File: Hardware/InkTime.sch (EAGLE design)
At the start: 105 parts, among them IC1 BQ25180YBGR, IC2 DRV2605YZFR, IC3 BMA423, IC9 RT6160AWSC, J1 503480-2400, J2 TC2030-IDC, J4 KH-TYPE-C-16P, Q1 20V/4.2A/52mΩ/1.4W, Q3 SI1308EDL-T1-GE3, U1 NRF52840_QF, U3 MAX17048G+T10, X1 32MHz, X2 32.768kHz

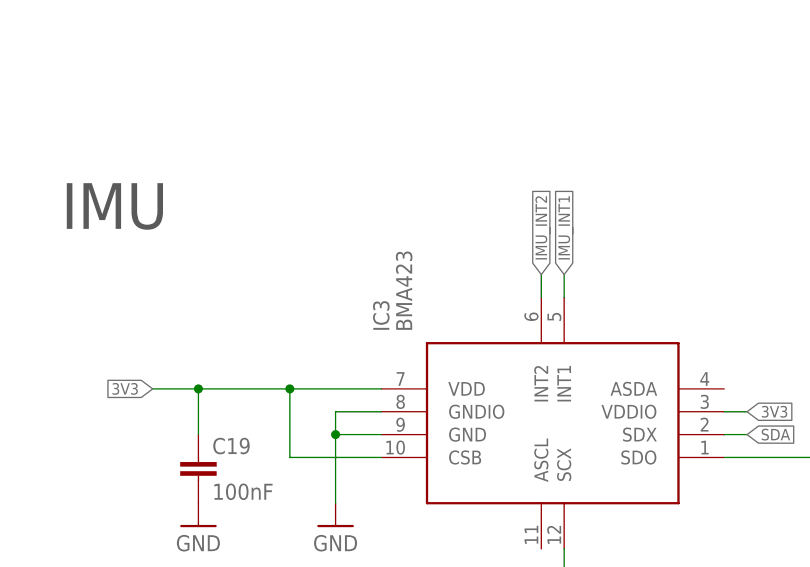
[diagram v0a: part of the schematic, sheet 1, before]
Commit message: fix: BMA423 -> BMA421
Signed-off-by: Luca Mazilescu <luca.mazilescu@protonmail.com>
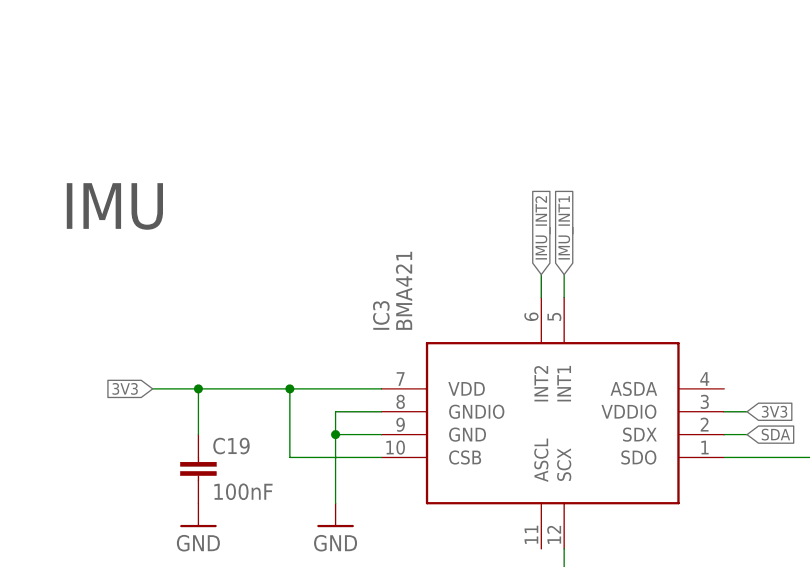
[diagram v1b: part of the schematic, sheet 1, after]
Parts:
- IC3: value BMA423 -> BMA421; device InkTime_v5:BMA423_BMA423 -> InkTime_v5:BMA421_BMA421
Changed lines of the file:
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@@
 <grid distance="0.1" unitdist="inch" unit="inch" style="lines" multiple="1" display="no" altdistance="0.01" altunitdist="inch" altunit="inch"/>
 <layers>
-<layer number="1" name="Top" color="4" fill="1" visible="no" active="no"/>
-<layer number="2" name="Route2" color="16" fill="1" visible="no" active="no"/>
-<layer number="3" name="Route3" color="17" fill="1" visible="no" active="no"/>
-<layer number="4" name="Route4" color="18" fill="1" visible="no" active="no"/>
-<layer number="5" name="Route5" color="19" fill="1" visible="no" active="no"/>
-<layer number="6" name="Route6" color="25" fill="1" visible="no" active="no"/>
-<layer number="7" name="Route7" color="26" fill="1" visible="no" active="no"/>
-<layer number="8" name="Route8" color="27" fill="1" visible="no" active="no"/>
-<layer number="9" name="Route9" color="28" fill="1" visible="no" active="no"/>
-<layer number="10" name="Route10" color="29" fill="1" visible="no" active="no"/>
-<layer number="11" name="Route11" color="30" fill="1" visible="no" active="no"/>
-<layer number="12" name="Route12" color="20" fill="1" visible="no" active="no"/>
-<layer number="13" name="Route13" color="21" fill="1" visible="no" active="no"/>
-<layer number="14" name="Route14" color="22" fill="1" visible="no" active="no"/>
-<layer number="15" name="Route15" color="23" fill="1" visible="no" active="no"/>
-<layer number="16" name="Bottom" color="1" fill="1" visible="no" active="no"/>
-<layer number="17" name="Pads" color="2" fill="1" visible="no" active="no"/>
-<layer number="18" name="Vias" color="2" fill="1" visible="no" active="no"/>
-<layer number="19" name="Unrouted" color="6" fill="1" visible="no" active="no"/>
-<layer number="20" name="Dimension" color="24" fill="1" visible="no" active="no"/>
-<layer number="21" name="tPlace" color="7" fill="1" visible="no" active="no"/>
-<layer number="22" name="bPlace" color="7" fill="1" visible="no" active="no"/>
-<layer number="23" name="tOrigins" color="15" fill="1" visible="no" active="no"/>
-<layer number="24" name="bOrigins" color="15" fill="1" visible="no" active="no"/>
-<layer number="25" name="tNames" color="7" fill="1" visible="no" active="no"/>
-<layer number="26" name="bNames" color="7" fill="1" visible="no" active="no"/>
-<layer number="27" name="tValues" color="7" fill="1" visible="no" active="no"/>
-<layer number="28" name="bValues" color="7" fill="1" visible="no" active="no"/>
+<layer number="1" name="Top" color="4" fill="1" visible="yes" active="no"/>
+<layer number="2" name="Route2" color="16" fill="1" visible="yes" active="no"/>
+<layer number="3" name="Route3" color="17" fill="1" visible="yes" active="no"/>
+<layer number="4" name="Route4" color="18" fill="1" visible="yes" active="no"/>
+<layer number="5" name="Route5" color="19" fill="1" visible="yes" active="no"/>
+<layer number="6" name="Route6" color="25" fill="1" visible="yes" active="no"/>
+<layer number="7" name="Route7" color="26" fill="1" visible="yes" active="no"/>
+<layer number="8" name="Route8" color="27" fill="1" visible="yes" active="no"/>
+<layer number="9" name="Route9" color="28" fill="1" visible="yes" active="no"/>
+<layer number="10" name="Route10" color="29" fill="1" visible="yes" active="no"/>
+<layer number="11" name="Route11" color="30" fill="1" visible="yes" active="no"/>
+<layer number="12" name="Route12" color="20" fill="1" visible="yes" active="no"/>
+<layer number="13" name="Route13" color="21" fill="1" visible="yes" active="no"/>
+<layer number="14" name="Route14" color="22" fill="1" visible="yes" active="no"/>
+<layer number="15" name="Route15" color="23" fill="1" visible="yes" active="no"/>
+<layer number="16" name="Bottom" color="1" fill="1" visible="yes" active="no"/>
+<layer number="17" name="Pads" color="2" fill="1" visible="yes" active="no"/>
+<layer number="18" name="Vias" color="2" fill="1" visible="yes" active="no"/>
+<layer number="19" name="Unrouted" color="6" fill="1" visible="yes" active="no"/>
+<layer number="20" name="Dimension" color="24" fill="1" visible="yes" active="no"/>
+<layer number="21" name="tPlace" color="7" fill="1" visible="yes" active="no"/>
+<layer number="22" name="bPlace" color="7" fill="1" visible="yes" active="no"/>
+<layer number="23" name="tOrigins" color="15" fill="1" visible="yes" active="no"/>
+<layer number="24" name="bOrigins" color="15" fill="1" visible="yes" active="no"/>
+<layer number="25" name="tNames" color="7" fill="1" visible="yes" active="no"/>
+<layer number="26" name="bNames" color="7" fill="1" visible="yes" active="no"/>
+<layer number="27" name="tValues" color="7" fill="1" visible="yes" active="no"/>
+<layer number="28" name="bValues" color="7" fill="1" visible="yes" active="no"/>
 <layer number="29" name="tStop" color="7" fill="3" visible="no" active="no"/>
 <layer number="30" name="bStop" color="7" fill="6" visible="no" active="no"/>
@@
 <layer number="35" name="tGlue" color="7" fill="4" visible="no" active="no"/>
 <layer number="36" name="bGlue" color="7" fill="5" visible="no" active="no"/>
-<layer number="37" name="tTest" color="7" fill="1" visible="no" active="no"/>
-<layer number="38" name="bTest" color="7" fill="1" visible="no" active="no"/>
+<layer number="37" name="tTest" color="7" fill="1" visible="yes" active="no"/>
+<layer number="38" name="bTest" color="7" fill="1" visible="yes" active="no"/>
 <layer number="39" name="tKeepout" color="4" fill="11" visible="no" active="no"/>
 <layer number="40" name="bKeepout" color="1" fill="11" visible="no" active="no"/>
@@
 <layer number="44" name="Drills" color="7" fill="1" visible="no" active="no"/>
 <layer number="45" name="Holes" color="7" fill="1" visible="no" active="no"/>
-<layer number="46" name="Milling" color="3" fill="1" visible="no" active="no"/>
-<layer number="47" name="Measures" color="7" fill="1" visible="no" active="no"/>
-<layer number="48" name="Document" color="7" fill="1" visible="no" active="no"/>
-<layer number="49" name="Reference" color="7" fill="1" visible="no" active="no"/>
-<layer number="51" name="tDocu" color="7" fill="1" visible="no" active="no"/>
-<layer number="52" name="bDocu" color="7" fill="1" visible="no" active="no"/>
+<layer number="46" name="Milling" color="3" fill="1" visible="yes" active="no"/>
+<layer number="47" name="Measures" color="7" fill="1" visible="yes" active="no"/>
+<layer number="48" name="Document" color="7" fill="1" visible="yes" active="no"/>
+<layer number="49" name="Reference" color="7" fill="1" visible="yes" active="no"/>
+<layer number="51" name="tDocu" color="7" fill="1" visible="yes" active="no"/>
+<layer number="52" name="bDocu" color="7" fill="1" visible="yes" active="no"/>
 <layer number="88" name="SimResults" color="9" fill="1" visible="yes" active="yes"/>
 <layer number="89" name="SimProbes" color="9" fill="1" visible="yes" active="yes"/>
@@
 <part name="R17" library="InkTime_v5" library_urn="urn:adsk.wipprod:fs.file:vf.8BTbcW1WSFWj7_HBs_dgew" deviceset="CPF0201D7K68C1_CPF0201D7K68C1" device="" value="3K3"/>
 <part name="R18" library="InkTime_v5" library_urn="urn:adsk.wipprod:fs.file:vf.8BTbcW1WSFWj7_HBs_dgew" deviceset="CPF0201D7K68C1_CPF0201D7K68C1" device="" value="3K3"/>
-<part name="IC3" library="InkTime_v5" library_urn="urn:adsk.wipprod:fs.file:vf.8BTbcW1WSFWj7_HBs_dgew" deviceset="BMA423_BMA423" device="" value="BMA423"/>
+<part name="IC3" library="InkTime_v5" library_urn="urn:adsk.wipprod:fs.file:vf.8BTbcW1WSFWj7_HBs_dgew" deviceset="BMA421_BMA421" device="" value="BMA421"/>
 <part name="SUPPLY28" library="InkTime_v5" library_urn="urn:adsk.wipprod:fs.file:vf.8BTbcW1WSFWj7_HBs_dgew" deviceset="POWER_SYMBOLS_GND-BAR" device="" value="GND"/>
 <part name="SUPPLY29" library="InkTime_v5" library_urn="urn:adsk.wipprod:fs.file:vf.8BTbcW1WSFWj7_HBs_dgew" deviceset="POWER_SYMBOLS_GND-BAR" device="" value="GND"/>

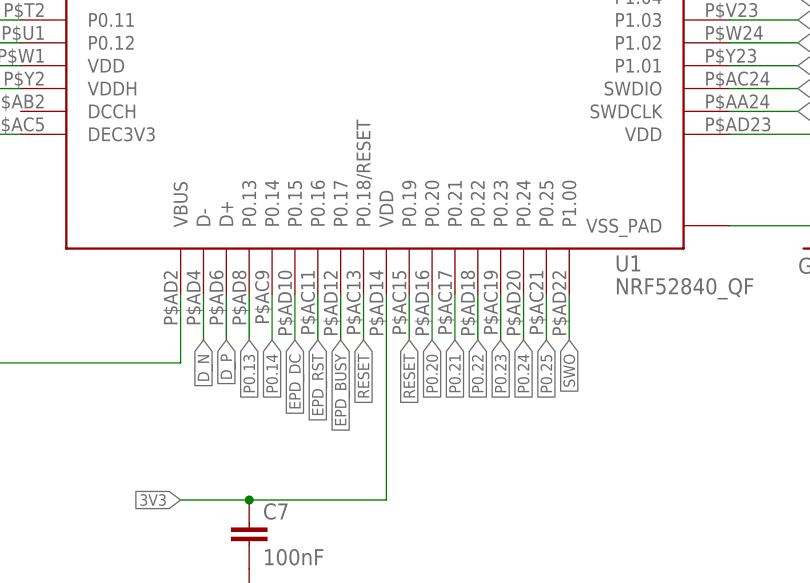
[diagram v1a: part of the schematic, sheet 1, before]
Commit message: fix: mask P0.19 from nRF package
Signed-off-by: Luca Mazilescu <luca.mazilescu@protonmail.com>
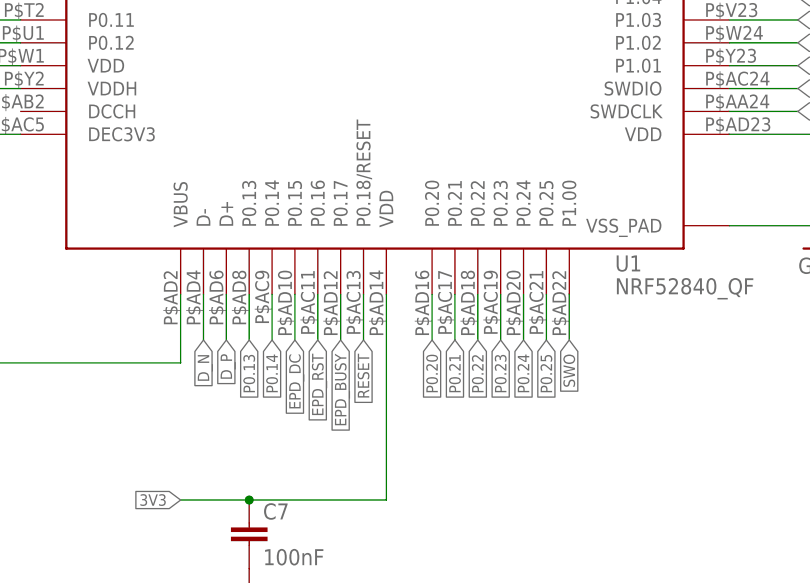
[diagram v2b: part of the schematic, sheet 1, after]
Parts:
- U1: device InkTime_v5:NORDIC_NRF_4_NRF52840_QF_PINCLEAN -> InkTime_v5:NORDIC_NRF_4_NRF52840_QF_PINCLEAN2
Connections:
- net RESET: no longer U1.P0.19@AC15
